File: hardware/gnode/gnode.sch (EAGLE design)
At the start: 25 parts, among them IC1 HTU21D, U1 ATMEGA328P_TQFP

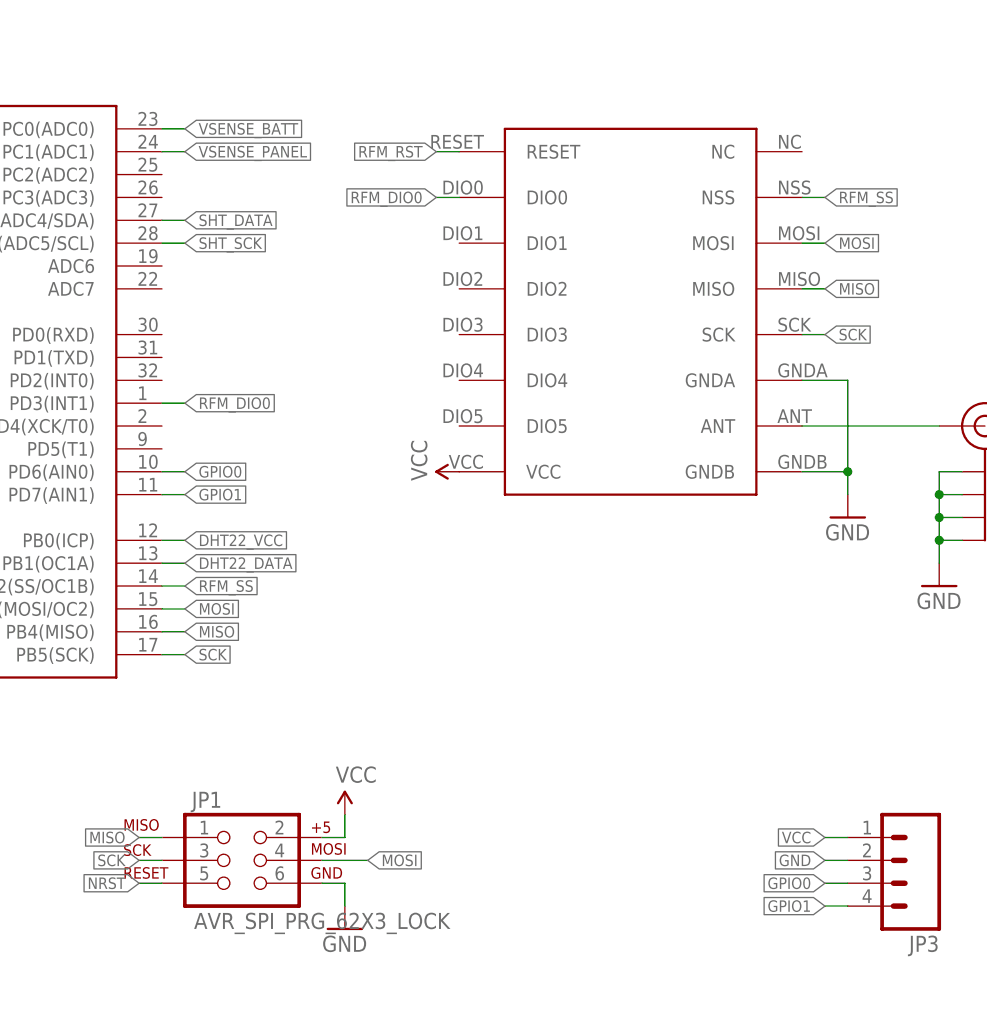
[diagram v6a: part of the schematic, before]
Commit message: routed gpio for adc/pwm
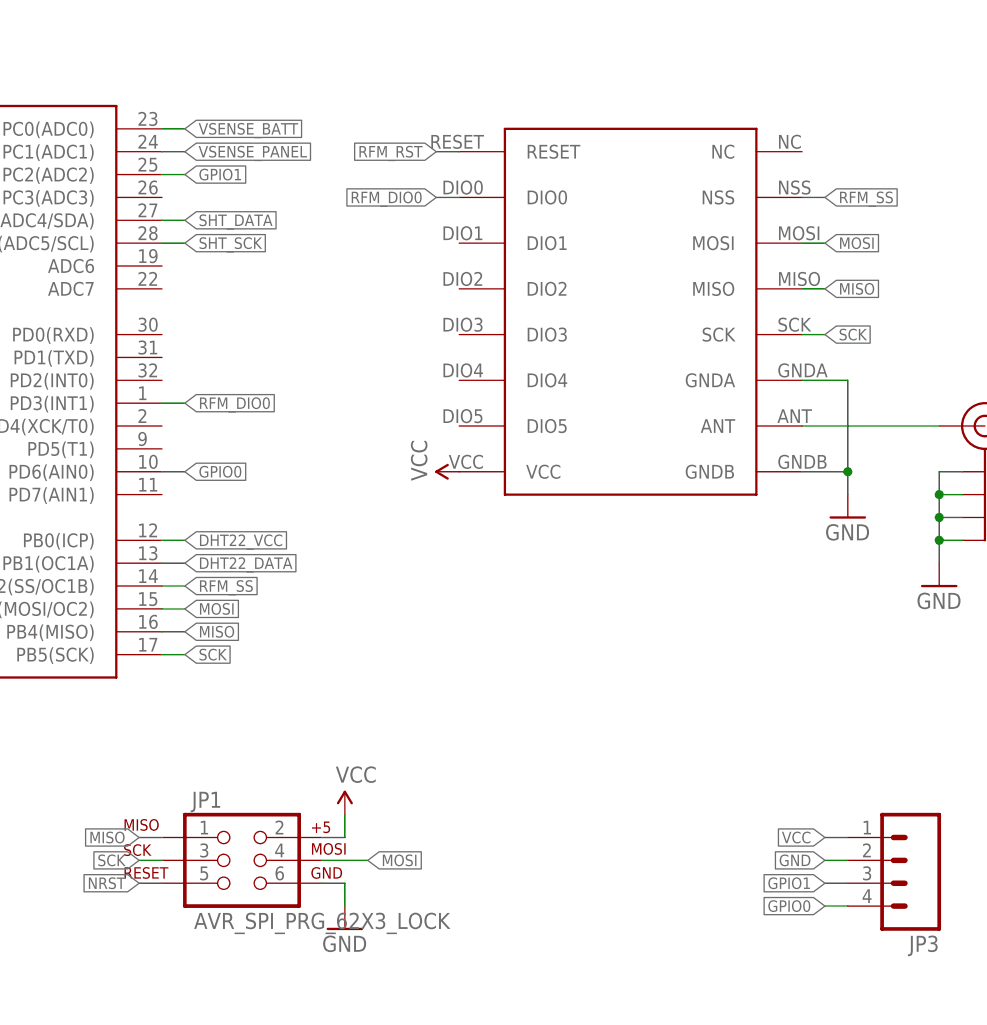
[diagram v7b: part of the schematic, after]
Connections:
- net GPIO0: now also JP3.4; no longer JP3.3
- net GPIO1: now also JP3.3, U1.PC2(ADC2); no longer JP3.4, U1.PD7(AIN1)
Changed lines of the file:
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@@
 <?xml version="1.0" encoding="utf-8"?>
 <!DOCTYPE eagle SYSTEM "eagle.dtd">
-<eagle version="6.5.0">
+<eagle version="6.6.0">
 <drawing>
 <settings>
@@
 <net name="GPIO1" class="0">
 <segment>
-<pinref part="U1" gate="U$1" pin="PD7(AIN1)"/>
-<wire x1="12.7" y1="25.4" x2="15.24" y2="25.4" width="0.1524" layer="91"/>
-<label x="15.24" y="25.4" size="1.27" layer="95" xref="yes"/>
+<pinref part="U1" gate="U$1" pin="PC2(ADC2)"/>
+<wire x1="12.7" y1="60.96" x2="15.24" y2="60.96" width="0.1524" layer="91"/>
+<label x="15.24" y="60.96" size="1.27" layer="95" xref="yes"/>
+</segment>
+<segment>
+<pinref part="JP3" gate="G$1" pin="3"/>
+<wire x1="88.9" y1="-17.78" x2="86.36" y2="-17.78" width="0.1524" layer="91"/>
+<label x="86.36" y="-17.78" size="1.27" layer="95" rot="R180" xref="yes"/>
+</segment>
+</net>
+<net name="GPIO0" class="0">
+<segment>
+<pinref part="U1" gate="U$1" pin="PD6(AIN0)"/>
+<wire x1="12.7" y1="27.94" x2="15.24" y2="27.94" width="0.1524" layer="91"/>
+<label x="15.24" y="27.94" size="1.27" layer="95" xref="yes"/>
 </segment>
 <segment>
@@
 </segment>
 </net>
-<net name="GPIO0" class="0">
-<segment>
-<pinref part="U1" gate="U$1" pin="PD6(AIN0)"/>
-<wire x1="12.7" y1="27.94" x2="15.24" y2="27.94" width="0.1524" layer="91"/>
-<label x="15.24" y="27.94" size="1.27" layer="95" xref="yes"/>
-</segment>
-<segment>
-<pinref part="JP3" gate="G$1" pin="3"/>
-<wire x1="88.9" y1="-17.78" x2="86.36" y2="-17.78" width="0.1524" layer="91"/>
-<label x="86.36" y="-17.78" size="1.27" layer="95" rot="R180" xref="yes"/>
-</segment>
-</net>
